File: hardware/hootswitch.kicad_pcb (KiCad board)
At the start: 2 copper layers, 100 x 88 mm, 127 parts, among them J1 Mini-DIN-4-G, J10 POWSEL, J11 TWI, J12 TWI, J2 Mini-DIN-4-G, J3 Mini-DIN-4-G, J4 Mini-DIN-4-G, J5 Mini-DIN-4-G, J6 Mini-DIN-4-G, J7 Barrel_Jack_MountingPin, J8 EXT_POW, J9 SW1, Q1 MMBT3904, Q10 MMBT3904, Q11 MMBT3904, Q12 MMBT3904, Q13 MMBT3904, Q14 MMBT3904, Q15 MMBT3904, Q16 MMBT3904, Q2 MMBT3904, Q3 MMBT3904, Q4 MMBT3904, Q5 MMBT3904, Q6 MMBT3904, Q7 MMBT3904, Q8 MMBT3904, Q9 MMBT3904, SW1 Switch1, U1 Pico, U10 LTV-357T, U11 LTV-357T, U2 LM1117-5.0, U3 ADuM1201AR, U4 ADuM1201AR, U5 ADuM1201AR, U6 ADuM1201AR, U7 ADuM1201AR, U8 LTV-357T, U9 LTV-357T

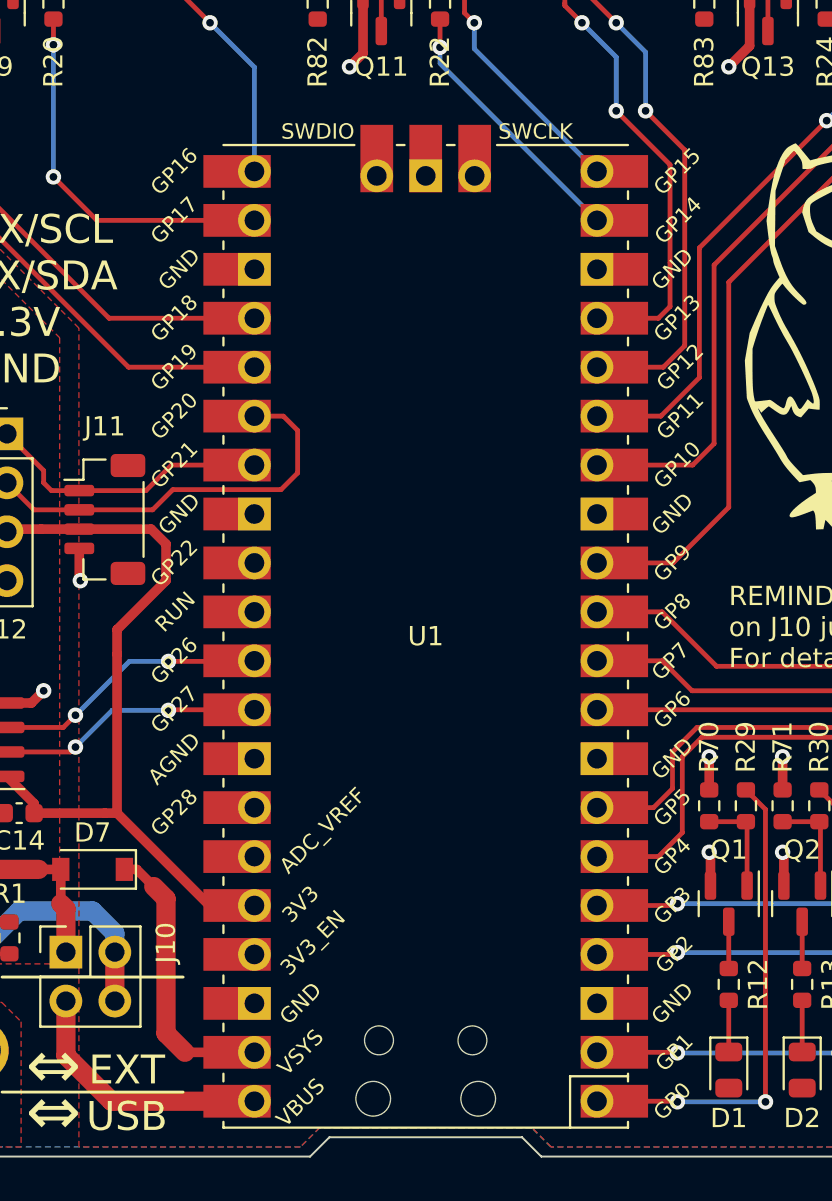
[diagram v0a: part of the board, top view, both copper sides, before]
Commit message: Switch to using the RPi provided PicoW symbol and footprint.
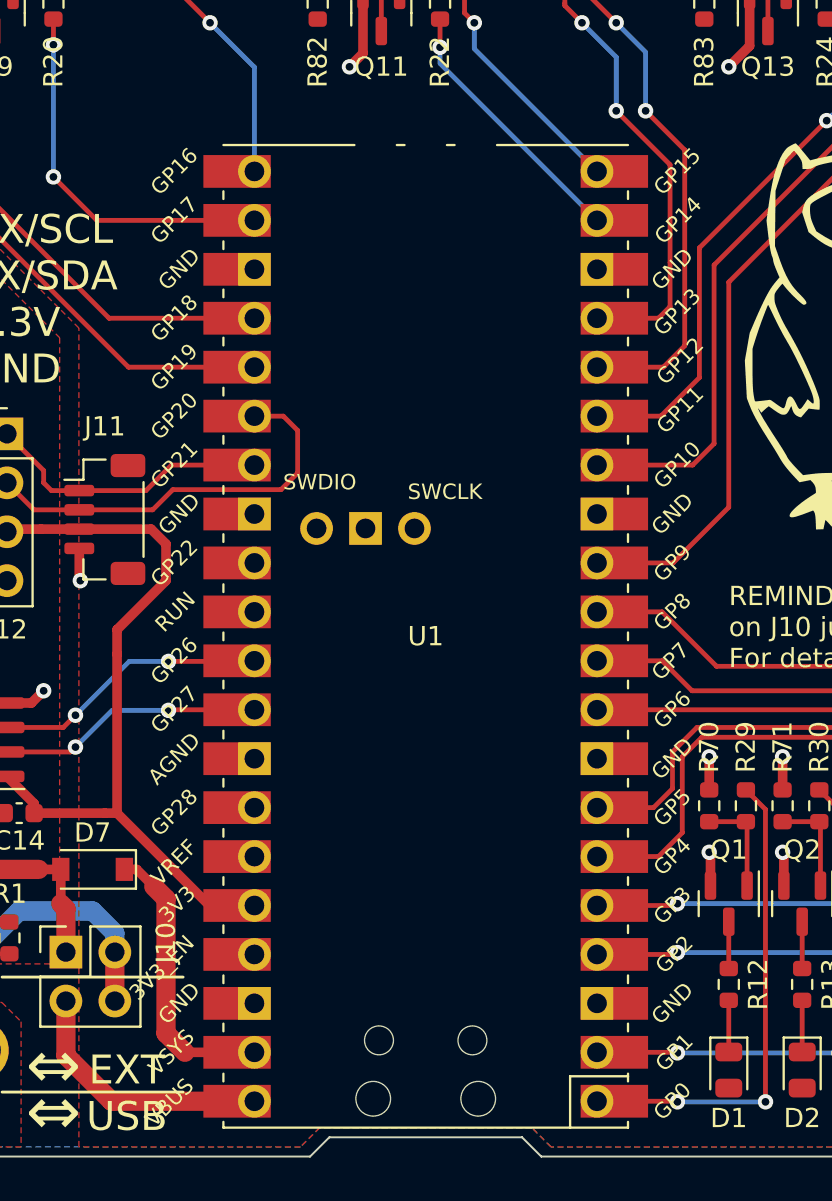
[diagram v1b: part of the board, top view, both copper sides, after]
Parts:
- U1: value Pico -> PicoW; footprint MCU_RaspberryPi_and_Boards:RPi_Pico_SMD_TH -> RPi_Pico:RPi_PicoW_SMD_TH
